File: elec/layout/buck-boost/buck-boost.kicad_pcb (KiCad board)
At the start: 6 copper layers, 69 parts, among them U10 2.49kΩ ±1% 62.5mW, U11 4.7µF ±10% 100V X7R, U12 4.7µF ±10% 100V X7R, U13 4.7µF ±10% 100V X7R, U14 10µF ±10% 100V X7R, U15 10µF ±10% 100V X7R, U16 10µF ±10% 100V X7R, U17 10µF ±10% 100V X7R, U18 1µF ±10% 100V X7R, U19 100nF ±10% 100V X7R, U2 100nF ±10% 50V X7R, U20 100pF ±5% 100V C0G, U21 470nF ±20% 16V X5R, U22 100nF ±10% 16V X7R, U23 10Ω ±1% 62.5mW, U24 100nF ±10% 16V X7R, U25 10Ω ±1% 62.5mW, U26 5mΩ ±1% 1W, U27 4.7µF ±10% 100V X7R, U28 4.7µF ±10% 100V X7R, U29 4.7µF ±10% 100V X7R, U3 100nF ±10% 50V X7R, U30 10µF ±10% 100V X7R, U31 10µF ±10% 100V X7R, U32 10µF ±10% 100V X7R, U33 10µF ±10% 100V X7R, U34 1µF ±10% 100V X7R, U35 100nF ±10% 100V X7R, U36 100pF ±5% 100V C0G, U37 470nF ±20% 16V X5R, U38 100nF ±10% 16V X7R, U39 10Ω ±1% 62.5mW, U4 50kΩ ±1% 62.5mW, U40 100nF ±10% 16V X7R, U41 10Ω ±1% 62.5mW, U42 5mΩ ±1% 1W, U43 13.7kΩ ±1% 62.5mW, U44 249kΩ ±0%, U45 1MΩ ±1% 100mW, U46 133kΩ ±1% 100mW, U47 25.5kΩ ±0% 100mW, U48 4.7µF ±10% 25V X5R, U49 100nF ±10% 100V X7R, U50 1µF ±10% 100V X7R, U51 4.7µF ±10% 100V X7R, U52 4.7µF ±10% 100V X7R, U54 0Ω 62.5mW, U58 30.1kΩ ±1% 62.5mW, U59 5.23kΩ ±1% 62.5mW, U9 4.7µF ±10% 25V X5R

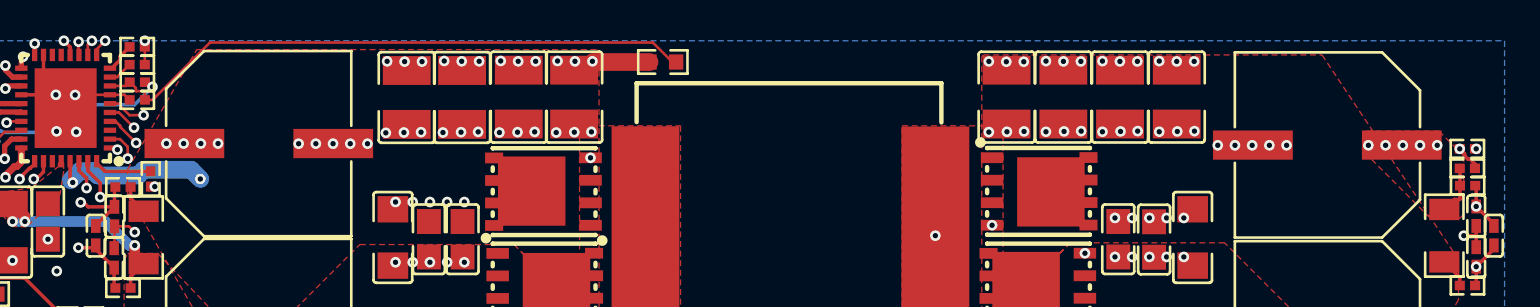
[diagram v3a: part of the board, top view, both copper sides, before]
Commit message: update syntax, delete vendored packages
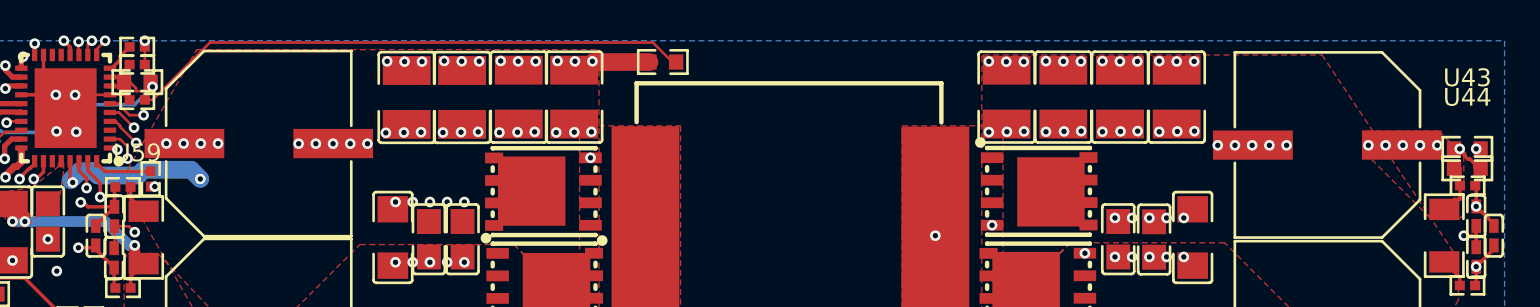
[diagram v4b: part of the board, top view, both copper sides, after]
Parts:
- U14, U15, U16, U17, U30, U31, U32, U33: value 10µF ±10% 100V X7R -> 10µF ±10% 100V X7S
- U43: value 13.7kΩ ±1% 62.5mW -> 13.7kΩ ±1% 100mW; footprint atopile:R0402-56259e -> atopile:R0603-ebcab9
- U44: value 249kΩ ±0% -> 249kΩ ±1% 100mW; footprint atopile:R0402-56259e -> atopile:R0603-ebcab9
- U59: value 5.23kΩ ±1% 62.5mW -> 5.23kΩ ±1% 100mW; footprint atopile:R0402-56259e -> atopile:R0603-ebcab9
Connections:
- C1 pad 1: hv-1 -> hv-3
- C2 pad 1: hv -> hv-2
- C3 pad 1: hv-3 -> hv-1
- C4 pad 1: hv-2 -> hv
- DS1 pad 1: cathode-1 -> cathode
- DS2 pad 1: cathode -> cathode-1
- Q1 pad 4: line-3 -> gate-2
- Q1 pad 5: hv-1 -> hv-3
- Q1 pad 6: hv-1 -> hv-3
- Q1 pad 7: hv-1 -> hv-3
- Q1 pad 8: hv-1 -> hv-3
- Q2 pad 4: line-6 -> gate
- Q3 pad 4: gate -> line-5
- Q3 pad 5: hv -> hv-2
- Q3 pad 6: hv -> hv-2
- Q3 pad 7: hv -> hv-2
- Q3 pad 8: hv -> hv-2
- R1 pad 2: gnd-4 -> gnd-1
- R2 pad 2: gnd-3 -> gnd-2
- R3 pad 2: gnd-2 -> gnd-4
- U1 pad 11: gnd-1 -> output_v_sense-gnd
- U1 pad 13: line -> line-3
- U1 pad 14: line-1 -> line
- U1 pad 19: gate -> line-5
- U1 pad 20: cathode -> cathode-1
- U1 pad 25: line-6 -> gate
- U1 pad 26: cathode-1 -> cathode
- U1 pad 27: line-3 -> gate-2
- U1 pad 30: line-5 -> line-1
- U1 pad 32: hv-3 -> hv-1
- U1 pad 33: hv-2 -> hv
- U1 pad 4: gnd-3 -> gnd-2
- U1 pad 5: gnd-2 -> gnd-4
- U1 pad 6: gnd-4 -> gnd-1
- U11 pad 1: hv-1 -> hv-3
- U12 pad 1: hv-1 -> hv-3
- U13 pad 1: hv-1 -> hv-3
- U14 pad 1: hv-1 -> hv-3
- U15 pad 1: hv-1 -> hv-3
- U16 pad 1: hv-1 -> hv-3
- U17 pad 1: hv-1 -> hv-3
- U18 pad 1: hv-1 -> hv-3
- U19 pad 1: hv-1 -> hv-3
- U2 pad 2: cathode-1 -> cathode
- U20 pad 1: hv-1 -> hv-3
- U21 pad 1: line-5 -> line-1
- U23 pad 1: hv-1 -> hv-3
- U24 pad 1: line-5 -> line-1
- U25 pad 1: hv-3 -> hv-1
- U25 pad 2: line-5 -> line-1
- U26 pad 1: hv-3 -> hv-1
- U26 pad 2: hv-1 -> hv-3
- U27 pad 1: hv -> hv-2
- U28 pad 1: hv -> hv-2
- U29 pad 1: hv -> hv-2
- U3 pad 2: cathode -> cathode-1
- U30 pad 1: hv -> hv-2
- U31 pad 1: hv -> hv-2
- U32 pad 1: hv -> hv-2
- U33 pad 1: hv -> hv-2
- U34 pad 1: hv -> hv-2
- U35 pad 1: hv -> hv-2
- U36 pad 1: hv -> hv-2
- U37 pad 1: line-1 -> line
- U37 pad 2: line -> line-3
- U38 pad 1: line -> line-3
- U39 pad 1: hv-2 -> hv
- U39 pad 2: line -> line-3
- U40 pad 1: line-1 -> line
- U41 pad 1: hv -> hv-2
- U41 pad 2: line-1 -> line
- U42 pad 1: hv -> hv-2
- U42 pad 2: hv-2 -> hv
- U43 pad 2: gnd-1 -> output_v_sense-gnd
- U44 pad 1: hv-2 -> hv
- U45 pad 1: hv-3 -> hv-1
- U49 pad 1: hv-3 -> hv-1
- U50 pad 1: hv-3 -> hv-1
- U51 pad 1: hv-1 -> hv-3
- U52 pad 1: hv -> hv-2
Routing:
- net output_v_sense-gnd: track 0.00 -> 81.7 mm, vias 0 -> 2
- net line-1: track 88.9 -> 10.1 mm
- net hv-2: track 78.8 -> 1.69 mm, vias 7 -> 34
- net hv: track 1.69 -> 78.8 mm, vias 34 -> 7
- net gnd-1: track 81.7 -> 17.4 mm
- net line-5: track 10.1 -> 59.3 mm
- net line-3: track 37.8 -> 86.4 mm
- net line-6: track 38.0 -> 0.00 mm, vias 2 -> 0
- net gate-2: track 0.00 -> 37.8 mm, vias 0 -> 2
- net hv-3: track 27.9 -> 1.67 mm, vias 8 -> 33
- net hv-1: track 1.67 -> 27.9 mm, vias 33 -> 8
- net gate: track 59.3 -> 38.0 mm
- net gnd-3: track 12.5 -> 0.00 mm, vias 2 -> 0
- net gnd-2: track 15.6 -> 12.5 mm
- net cathode-1: track 59.5 -> 62.4 mm
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- added copper zone on In2.Cu, net hv-2
- added copper zone on In2.Cu, net hv-3
- removed copper zone on In2.Cu, net hv
- removed copper zone on In2.Cu, net hv-1

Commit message: build and re-link layouts
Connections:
- net gnd-1 renamed gnd-3
- C1 pad 1: hv-3 -> hv-2
- C1 pad 2: gnd -> gnd-2
- C2 pad 1: hv-2 -> hv-1
- C2 pad 2: gnd -> gnd-2
- C3 pad 1: hv-1 -> hv
- C3 pad 2: gnd -> gnd-2
- C4 pad 1: hv -> hv-3
- C4 pad 2: gnd -> gnd-2
- DS1 pad 1: cathode -> cathode-1
- DS1 pad 2: anode -> anode-1
- DS2 pad 1: cathode-1 -> cathode
- DS2 pad 2: anode -> anode-1
- Q1 pad 4: gate-2 -> gate
- Q1 pad 5: hv-3 -> hv-2
- Q1 pad 6: hv-3 -> hv-2
- Q1 pad 7: hv-3 -> hv-2
- Q1 pad 8: hv-3 -> hv-2
- Q2 pad 1: gnd -> gnd-2
- Q2 pad 2: gnd -> gnd-2
- Q2 pad 3: gnd -> gnd-2
- Q2 pad 4: gate -> line-7
- Q3 pad 1: drain -> line-4
- Q3 pad 2: drain -> line-4
- Q3 pad 3: drain -> line-4
- Q3 pad 4: line-5 -> line
- Q3 pad 5: hv-2 -> hv-1
- Q3 pad 6: hv-2 -> hv-1
- Q3 pad 7: hv-2 -> hv-1
- Q3 pad 8: hv-2 -> hv-1
- Q4 pad 1: gnd -> gnd-2
- Q4 pad 2: gnd -> gnd-2
- Q4 pad 3: gnd -> gnd-2
- Q4 pad 5: drain -> line-4
- Q4 pad 6: drain -> line-4
- Q4 pad 7: drain -> line-4
- Q4 pad 8: drain -> line-4
- R2 pad 2: gnd-2 -> gnd-4
- R3 pad 2: gnd-4 -> gnd
- U1 pad 13: line-3 -> line-5
- U1 pad 14: line -> line-1
- U1 pad 17: gnd -> gnd-2
- U1 pad 18: drain -> line-4
- U1 pad 19: line-5 -> line
- U1 pad 20: cathode-1 -> cathode
- U1 pad 22: gnd -> gnd-2
- U1 pad 23: anode -> anode-1
- U1 pad 24: anode-1 -> anode
- U1 pad 25: gate -> line-7
- U1 pad 26: cathode -> cathode-1
- U1 pad 27: gate-2 -> gate
- U1 pad 29: line-4 -> line-3
- U1 pad 30: line-1 -> line-6
- U1 pad 32: hv-1 -> hv
- U1 pad 33: hv -> hv-3
- U1 pad 37: gnd -> gnd-2
- U1 pad 4: gnd-2 -> gnd-4
- U1 pad 5: gnd-4 -> gnd
- U1 pad 7: gnd -> gnd-2
- U10 pad 2: gnd -> gnd-2
- U11 pad 1: hv-3 -> hv-2
- U11 pad 2: gnd -> gnd-2
- U12 pad 1: hv-3 -> hv-2
- U12 pad 2: gnd -> gnd-2
- U13 pad 1: hv-3 -> hv-2
- U13 pad 2: gnd -> gnd-2
- U14 pad 1: hv-3 -> hv-2
- U14 pad 2: gnd -> gnd-2
- U15 pad 1: hv-3 -> hv-2
- U15 pad 2: gnd -> gnd-2
- U16 pad 1: hv-3 -> hv-2
- U16 pad 2: gnd -> gnd-2
- U17 pad 1: hv-3 -> hv-2
- U17 pad 2: gnd -> gnd-2
- U18 pad 1: hv-3 -> hv-2
- U18 pad 2: gnd -> gnd-2
- U19 pad 1: hv-3 -> hv-2
- U19 pad 2: gnd -> gnd-2
- U2 pad 2: cathode -> cathode-1
- U20 pad 1: hv-3 -> hv-2
- U20 pad 2: gnd -> gnd-2
- U21 pad 1: line-1 -> line-6
- U21 pad 2: line-4 -> line-3
- U22 pad 1: line-4 -> line-3
- U22 pad 2: gnd -> gnd-2
- U23 pad 1: hv-3 -> hv-2
- U23 pad 2: line-4 -> line-3
- U24 pad 1: line-1 -> line-6
- U24 pad 2: gnd -> gnd-2
- U25 pad 1: hv-1 -> hv
- U25 pad 2: line-1 -> line-6
- U26 pad 1: hv-1 -> hv
- U26 pad 2: hv-3 -> hv-2
- U27 pad 1: hv-2 -> hv-1
- U27 pad 2: gnd -> gnd-2
- U28 pad 1: hv-2 -> hv-1
- U28 pad 2: gnd -> gnd-2
- U29 pad 1: hv-2 -> hv-1
- U29 pad 2: gnd -> gnd-2
- U3 pad 1: drain -> line-4
- U3 pad 2: cathode-1 -> cathode
- U30 pad 1: hv-2 -> hv-1
- U30 pad 2: gnd -> gnd-2
- U31 pad 1: hv-2 -> hv-1
- U31 pad 2: gnd -> gnd-2
- U32 pad 1: hv-2 -> hv-1
- U32 pad 2: gnd -> gnd-2
- U33 pad 1: hv-2 -> hv-1
- U33 pad 2: gnd -> gnd-2
- U34 pad 1: hv-2 -> hv-1
- U34 pad 2: gnd -> gnd-2
- U35 pad 1: hv-2 -> hv-1
- U35 pad 2: gnd -> gnd-2
- U36 pad 1: hv-2 -> hv-1
- U36 pad 2: gnd -> gnd-2
- U37 pad 1: line -> line-1
- U37 pad 2: line-3 -> line-5
- U38 pad 1: line-3 -> line-5
- U38 pad 2: gnd -> gnd-2
- U39 pad 1: hv -> hv-3
- U39 pad 2: line-3 -> line-5
- U4 pad 2: gnd -> gnd-2
- U40 pad 1: line -> line-1
- U40 pad 2: gnd -> gnd-2
- U41 pad 1: hv-2 -> hv-1
- U41 pad 2: line -> line-1
- U42 pad 1: hv-2 -> hv-1
- U42 pad 2: hv -> hv-3
- U44 pad 1: hv -> hv-3
- U45 pad 1: hv-1 -> hv
- U47 pad 2: gnd -> gnd-2
- U48 pad 1: anode-1 -> anode
- U48 pad 2: gnd -> gnd-2
- U49 pad 1: hv-1 -> hv
- U49 pad 2: gnd -> gnd-2
- U5 pad 2: anode-1 -> anode
- U50 pad 1: hv-1 -> hv
- U50 pad 2: gnd -> gnd-2
- U51 pad 1: hv-3 -> hv-2
- U51 pad 2: gnd -> gnd-2
- U52 pad 1: hv-2 -> hv-1
- U52 pad 2: gnd -> gnd-2
- U54 pad 2: gnd -> gnd-2
- U55 pad 2: anode-1 -> anode
- U57 pad 2: gnd -> gnd-2
- U58 pad 2: gnd -> gnd-2
- U59 pad 1: anode-1 -> anode
- U7 pad 2: anode-1 -> anode
- U8 pad 2: drain -> line-4
- U9 pad 1: anode -> anode-1
- U9 pad 2: gnd -> gnd-2
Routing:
- net line-1: track 10.1 -> 88.9 mm
- net hv-3: track 1.67 -> 78.8 mm, vias 33 -> 7
- net line-3: track 86.4 -> 10.5 mm
- net drain: track 68.3 -> 0.00 mm, vias 2 -> 0
- net line-4: track 10.5 -> 68.3 mm
- net hv: track 78.8 -> 27.9 mm, vias 7 -> 8
- net line-7: track 0.00 -> 38.0 mm, vias 0 -> 2
- net gate-2: track 37.8 -> 0.00 mm, vias 2 -> 0
- net anode-1: track 35.4 -> 70.3 mm, vias 3 -> 2
- net anode: track 70.3 -> 35.4 mm, vias 2 -> 3
- net line: track 88.9 -> 59.3 mm
- net line-5: track 59.3 -> 86.4 mm
- net hv-1: track 27.9 -> 1.69 mm, vias 8 -> 34
- net gnd-2: track 12.5 -> 24.6 mm, vias 2 -> 90
- net line-6: track 0.00 -> 10.1 mm, vias 0 -> 2
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- added copper zone on B.Cu, net gnd-2
- added copper zone on F.Cu, net gnd-2
- added copper zone on In1.Cu, net gnd-2
- added copper zone on In2.Cu, net hv-1
- added copper zone on F.Cu, net line-4
- removed copper zone on F.Cu, net drain
- removed copper zone on B.Cu, net gnd
- removed copper zone on F.Cu, net gnd
- removed copper zone on In1.Cu, net gnd
- removed copper zone on In2.Cu, net hv-3

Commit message: all modules building
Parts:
- U50: value 1µF ±10% 100V X7R -> 1µF ±10% 250V X7R; footprint atopile:C1206-f0a137 -> atopile:C1812-bfe9b0
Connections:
- C1 pad 1: hv-2 -> hv-1
- C1 pad 2: gnd-2 -> gnd-3
- C2 pad 1: hv-1 -> hv-3
- C2 pad 2: gnd-2 -> gnd-3
- C3 pad 2: gnd-2 -> gnd-3
- C4 pad 1: hv-3 -> hv-2
- C4 pad 2: gnd-2 -> gnd-3
- DS1 pad 1: cathode-1 -> cathode
- DS2 pad 1: cathode -> cathode-1
- Q1 pad 1: line-2 -> drain
- Q1 pad 2: line-2 -> drain
- Q1 pad 3: line-2 -> drain
- Q1 pad 4: gate -> gate-2
- Q1 pad 5: hv-2 -> hv-1
- Q1 pad 6: hv-2 -> hv-1
- Q1 pad 7: hv-2 -> hv-1
- Q1 pad 8: hv-2 -> hv-1
- Q2 pad 1: gnd-2 -> gnd-3
- Q2 pad 2: gnd-2 -> gnd-3
- Q2 pad 3: gnd-2 -> gnd-3
- Q2 pad 4: line-7 -> gate
- Q2 pad 5: line-2 -> drain
- Q2 pad 6: line-2 -> drain
- Q2 pad 7: line-2 -> drain
- Q2 pad 8: line-2 -> drain
- Q3 pad 1: line-4 -> line
- Q3 pad 2: line-4 -> line
- Q3 pad 3: line-4 -> line
- Q3 pad 4: line -> gate-1
- Q3 pad 5: hv-1 -> hv-3
- Q3 pad 6: hv-1 -> hv-3
- Q3 pad 7: hv-1 -> hv-3
- Q3 pad 8: hv-1 -> hv-3
- Q4 pad 1: gnd-2 -> gnd-3
- Q4 pad 2: gnd-2 -> gnd-3
- Q4 pad 3: gnd-2 -> gnd-3
- Q4 pad 4: gate-1 -> line-4
- Q4 pad 5: line-4 -> line
- Q4 pad 6: line-4 -> line
- Q4 pad 7: line-4 -> line
- Q4 pad 8: line-4 -> line
- R1 pad 2: gnd-3 -> gnd-1
- U1 pad 13: line-5 -> line-1
- U1 pad 14: line-1 -> line-2
- U1 pad 17: gnd-2 -> gnd-3
- U1 pad 18: line-4 -> line
- U1 pad 19: line -> gate-1
- U1 pad 20: cathode -> cathode-1
- U1 pad 21: gate-1 -> line-4
- U1 pad 22: gnd-2 -> gnd-3
- U1 pad 25: line-7 -> gate
- U1 pad 26: cathode-1 -> cathode
- U1 pad 27: gate -> gate-2
- U1 pad 28: line-2 -> drain
- U1 pad 30: line-6 -> line-5
- U1 pad 33: hv-3 -> hv-2
- U1 pad 37: gnd-2 -> gnd-3
- U1 pad 6: gnd-3 -> gnd-1
- U1 pad 7: gnd-2 -> gnd-3
- U10 pad 2: gnd-2 -> gnd-3
- U11 pad 1: hv-2 -> hv-1
- U11 pad 2: gnd-2 -> gnd-3
- U12 pad 1: hv-2 -> hv-1
- U12 pad 2: gnd-2 -> gnd-3
- U13 pad 1: hv-2 -> hv-1
- U13 pad 2: gnd-2 -> gnd-3
- U14 pad 1: hv-2 -> hv-1
- U14 pad 2: gnd-2 -> gnd-3
- U15 pad 1: hv-2 -> hv-1
- U15 pad 2: gnd-2 -> gnd-3
- U16 pad 1: hv-2 -> hv-1
- U16 pad 2: gnd-2 -> gnd-3
- U17 pad 1: hv-2 -> hv-1
- U17 pad 2: gnd-2 -> gnd-3
- U18 pad 1: hv-2 -> hv-1
- U18 pad 2: gnd-2 -> gnd-3
- U19 pad 1: hv-2 -> hv-1
- U19 pad 2: gnd-2 -> gnd-3
- U2 pad 1: line-2 -> drain
- U2 pad 2: cathode-1 -> cathode
- U20 pad 1: hv-2 -> hv-1
- U20 pad 2: gnd-2 -> gnd-3
- U21 pad 1: line-6 -> line-5
- U22 pad 2: gnd-2 -> gnd-3
- U23 pad 1: hv-2 -> hv-1
- U24 pad 1: line-6 -> line-5
- U24 pad 2: gnd-2 -> gnd-3
- U25 pad 2: line-6 -> line-5
- U26 pad 2: hv-2 -> hv-1
- U27 pad 1: hv-1 -> hv-3
- U27 pad 2: gnd-2 -> gnd-3
- U28 pad 1: hv-1 -> hv-3
- U28 pad 2: gnd-2 -> gnd-3
- U29 pad 1: hv-1 -> hv-3
- U29 pad 2: gnd-2 -> gnd-3
- U3 pad 1: line-4 -> line
- U3 pad 2: cathode -> cathode-1
- U30 pad 1: hv-1 -> hv-3
- U30 pad 2: gnd-2 -> gnd-3
- U31 pad 1: hv-1 -> hv-3
- U31 pad 2: gnd-2 -> gnd-3
- U32 pad 1: hv-1 -> hv-3
- U32 pad 2: gnd-2 -> gnd-3
- U33 pad 1: hv-1 -> hv-3
- U33 pad 2: gnd-2 -> gnd-3
- U34 pad 1: hv-1 -> hv-3
- U34 pad 2: gnd-2 -> gnd-3
- U35 pad 1: hv-1 -> hv-3
- U35 pad 2: gnd-2 -> gnd-3
- U36 pad 1: hv-1 -> hv-3
- U36 pad 2: gnd-2 -> gnd-3
- U37 pad 1: line-1 -> line-2
- U37 pad 2: line-5 -> line-1
- U38 pad 1: line-5 -> line-1
- U38 pad 2: gnd-2 -> gnd-3
- U39 pad 1: hv-3 -> hv-2
- U39 pad 2: line-5 -> line-1
- U4 pad 2: gnd-2 -> gnd-3
- U40 pad 1: line-1 -> line-2
- U40 pad 2: gnd-2 -> gnd-3
- U41 pad 1: hv-1 -> hv-3
- U41 pad 2: line-1 -> line-2
- U42 pad 1: hv-1 -> hv-3
- U42 pad 2: hv-3 -> hv-2
- U44 pad 1: hv-3 -> hv-2
- U47 pad 2: gnd-2 -> gnd-3
- U48 pad 2: gnd-2 -> gnd-3
- U49 pad 2: gnd-2 -> gnd-3
- U50 pad 2: gnd-2 -> gnd-3
- U51 pad 1: hv-2 -> hv-1
- U51 pad 2: gnd-2 -> gnd-3
- U52 pad 1: hv-1 -> hv-3
- U52 pad 2: gnd-2 -> gnd-3
- U54 pad 2: gnd-2 -> gnd-3
- U57 pad 2: gnd-2 -> gnd-3
- U58 pad 2: gnd-2 -> gnd-3
- U8 pad 1: line-2 -> drain
- U8 pad 2: line-4 -> line
- U9 pad 2: gnd-2 -> gnd-3
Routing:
- net hv-2: track 1.67 -> 78.8 mm, vias 33 -> 7
- net hv-3: track 78.8 -> 1.69 mm, vias 7 -> 34
- net line-5: track 86.4 -> 10.1 mm
- net drain: track 0.00 -> 55.2 mm, vias 0 -> 3
- net line-7: track 38.0 -> 0.00 mm, vias 2 -> 0
- net gate-2: track 0.00 -> 37.8 mm, vias 0 -> 2
- net line-2: track 55.2 -> 88.9 mm, vias 3 -> 2
- net gnd-2: track 24.6 -> 0.00 mm, vias 90 -> 0
- net gnd-1: track 0.00 -> 17.4 mm, vias 0 -> 2
- net line-6: track 10.1 -> 0.00 mm, vias 2 -> 0
- net line: track 59.3 -> 68.3 mm
- net gate-1: track 67.3 -> 59.3 mm
- net gnd-3: track 17.4 -> 24.6 mm, vias 2 -> 90
- net cathode-1: track 59.5 -> 62.4 mm
- net cathode: track 62.4 -> 59.5 mm
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- added copper zone on F.Cu, net drain
- added copper zone on B.Cu, net gnd-3
- added copper zone on F.Cu, net gnd-3
- added copper zone on In1.Cu, net gnd-3
- added copper zone on In2.Cu, net hv-3
- added copper zone on F.Cu, net line
- removed copper zone on B.Cu, net gnd-2
- removed copper zone on F.Cu, net gnd-2
- removed copper zone on In1.Cu, net gnd-2
- removed copper zone on In2.Cu, net hv-2
- removed copper zone on F.Cu, net line-2
- removed copper zone on F.Cu, net line-4

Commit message: HIL Building
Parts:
- U43: value 13.7kΩ ±1% 100mW -> 13.7kΩ ±1% 62.5mW; footprint atopile:R0603-ebcab9 -> atopile:R0402-56259e
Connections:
- net gate-1 renamed line-6
- C1 pad 1: hv-1 -> hv
- C1 pad 2: gnd-3 -> gnd
- C2 pad 1: hv-3 -> hv-1
- C2 pad 2: gnd-3 -> gnd
- C3 pad 1: hv -> hv-3
- C3 pad 2: gnd-3 -> gnd
- C4 pad 2: gnd-3 -> gnd
- DS1 pad 1: cathode -> cathode-1
- DS2 pad 1: cathode-1 -> cathode
- Q1 pad 1: drain -> source
- Q1 pad 2: drain -> source
- Q1 pad 3: drain -> source
- Q1 pad 4: gate-2 -> line
- Q1 pad 5: hv-1 -> hv
- Q1 pad 6: hv-1 -> hv
- Q1 pad 7: hv-1 -> hv
- Q1 pad 8: hv-1 -> hv
- Q2 pad 1: gnd-3 -> gnd
- Q2 pad 2: gnd-3 -> gnd
- Q2 pad 3: gnd-3 -> gnd
- Q2 pad 4: gate -> line-2
- Q2 pad 5: drain -> source
- Q2 pad 6: drain -> source
- Q2 pad 7: drain -> source
- Q2 pad 8: drain -> source
- Q3 pad 1: line -> drain
- Q3 pad 2: line -> drain
- Q3 pad 3: line -> drain
- Q3 pad 5: hv-3 -> hv-1
- Q3 pad 6: hv-3 -> hv-1
- Q3 pad 7: hv-3 -> hv-1
- Q3 pad 8: hv-3 -> hv-1
- Q4 pad 1: gnd-3 -> gnd
- Q4 pad 2: gnd-3 -> gnd
- Q4 pad 3: gnd-3 -> gnd
- Q4 pad 4: line-4 -> gate
- Q4 pad 5: line -> drain
- Q4 pad 6: line -> drain
- Q4 pad 7: line -> drain
- Q4 pad 8: line -> drain
- R1 pad 2: gnd-1 -> gnd-2
- R2 pad 2: gnd-4 -> gnd-3
- R3 pad 2: gnd -> gnd-4
- U1 pad 11: output_v_sense-gnd -> gnd-1
- U1 pad 13: line-1 -> line-3
- U1 pad 14: line-2 -> line-1
- U1 pad 17: gnd-3 -> gnd
- U1 pad 18: line -> drain
- U1 pad 20: cathode-1 -> cathode
- U1 pad 21: line-4 -> gate
- U1 pad 22: gnd-3 -> gnd
- U1 pad 25: gate -> line-2
- U1 pad 26: cathode -> cathode-1
- U1 pad 27: gate-2 -> line
- U1 pad 28: drain -> source
- U1 pad 29: line-3 -> line-4
- U1 pad 32: hv -> hv-3
- U1 pad 37: gnd-3 -> gnd
- U1 pad 4: gnd-4 -> gnd-3
- U1 pad 5: gnd -> gnd-4
- U1 pad 6: gnd-1 -> gnd-2
- U1 pad 7: gnd-3 -> gnd
- U10 pad 2: gnd-3 -> gnd
- U11 pad 1: hv-1 -> hv
- U11 pad 2: gnd-3 -> gnd
- U12 pad 1: hv-1 -> hv
- U12 pad 2: gnd-3 -> gnd
- U13 pad 1: hv-1 -> hv
- U13 pad 2: gnd-3 -> gnd
- U14 pad 1: hv-1 -> hv
- U14 pad 2: gnd-3 -> gnd
- U15 pad 1: hv-1 -> hv
- U15 pad 2: gnd-3 -> gnd
- U16 pad 1: hv-1 -> hv
- U16 pad 2: gnd-3 -> gnd
- U17 pad 1: hv-1 -> hv
- U17 pad 2: gnd-3 -> gnd
- U18 pad 1: hv-1 -> hv
- U18 pad 2: gnd-3 -> gnd
- U19 pad 1: hv-1 -> hv
- U19 pad 2: gnd-3 -> gnd
- U2 pad 1: drain -> source
- U2 pad 2: cathode -> cathode-1
- U20 pad 1: hv-1 -> hv
- U20 pad 2: gnd-3 -> gnd
- U21 pad 2: line-3 -> line-4
- U22 pad 1: line-3 -> line-4
- U22 pad 2: gnd-3 -> gnd
- U23 pad 1: hv-1 -> hv
- U23 pad 2: line-3 -> line-4
- U24 pad 2: gnd-3 -> gnd
- U25 pad 1: hv -> hv-3
- U26 pad 1: hv -> hv-3
- U26 pad 2: hv-1 -> hv
- U27 pad 1: hv-3 -> hv-1
- U27 pad 2: gnd-3 -> gnd
- U28 pad 1: hv-3 -> hv-1
- U28 pad 2: gnd-3 -> gnd
- U29 pad 1: hv-3 -> hv-1
- U29 pad 2: gnd-3 -> gnd
- U3 pad 1: line -> drain
- U3 pad 2: cathode-1 -> cathode
- U30 pad 1: hv-3 -> hv-1
- U30 pad 2: gnd-3 -> gnd
- U31 pad 1: hv-3 -> hv-1
- U31 pad 2: gnd-3 -> gnd
- U32 pad 1: hv-3 -> hv-1
- U32 pad 2: gnd-3 -> gnd
- U33 pad 1: hv-3 -> hv-1
- U33 pad 2: gnd-3 -> gnd
- U34 pad 1: hv-3 -> hv-1
- U34 pad 2: gnd-3 -> gnd
- U35 pad 1: hv-3 -> hv-1
- U35 pad 2: gnd-3 -> gnd
- U36 pad 1: hv-3 -> hv-1
- U36 pad 2: gnd-3 -> gnd
- U37 pad 1: line-2 -> line-1
- U37 pad 2: line-1 -> line-3
- U38 pad 1: line-1 -> line-3
- U38 pad 2: gnd-3 -> gnd
- U39 pad 2: line-1 -> line-3
- U4 pad 2: gnd-3 -> gnd
- U40 pad 1: line-2 -> line-1
- U40 pad 2: gnd-3 -> gnd
- U41 pad 1: hv-3 -> hv-1
- U41 pad 2: line-2 -> line-1
- U42 pad 1: hv-3 -> hv-1
- U43 pad 2: output_v_sense-gnd -> gnd-1
- U45 pad 1: hv -> hv-3
- U47 pad 2: gnd-3 -> gnd
- U48 pad 2: gnd-3 -> gnd
- U49 pad 1: hv -> hv-3
- U49 pad 2: gnd-3 -> gnd
- U50 pad 1: hv -> hv-3
- U50 pad 2: gnd-3 -> gnd
- U51 pad 1: hv-1 -> hv
- U51 pad 2: gnd-3 -> gnd
- U52 pad 1: hv-3 -> hv-1
- U52 pad 2: gnd-3 -> gnd
- U54 pad 2: gnd-3 -> gnd
- U57 pad 2: gnd-3 -> gnd
- U58 pad 2: gnd-3 -> gnd
- U8 pad 1: drain -> source
- U8 pad 2: line -> drain
- U9 pad 2: gnd-3 -> gnd
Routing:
- net output_v_sense-gnd: track 81.7 -> 0.00 mm, vias 2 -> 0
- net line-3: track 10.5 -> 86.4 mm
- net gnd-1: track 17.4 -> 81.7 mm
- net line-4: track 67.3 -> 10.5 mm
- net source: track 0.00 -> 55.2 mm, vias 0 -> 3
- net line-2: track 88.9 -> 38.0 mm
- net gate-2: track 37.8 -> 0.00 mm, vias 2 -> 0
- net line: track 68.3 -> 37.8 mm
- net gate: track 38.0 -> 67.3 mm
- net hv: track 27.9 -> 1.67 mm, vias 8 -> 33
- net hv-3: track 1.69 -> 27.9 mm, vias 34 -> 8
- net gnd-2: track 0.00 -> 17.4 mm, vias 0 -> 2
- net drain: track 55.2 -> 68.3 mm, vias 3 -> 2
- net gnd-3: track 24.6 -> 12.5 mm, vias 90 -> 2
- net gnd: track 15.6 -> 24.6 mm, vias 2 -> 90
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- added copper zone on B.Cu, net gnd
- added copper zone on F.Cu, net gnd
- added copper zone on In1.Cu, net gnd
- added copper zone on In2.Cu, net hv
- added copper zone on F.Cu, net source
- removed copper zone on B.Cu, net gnd-3
- removed copper zone on F.Cu, net gnd-3
- removed copper zone on In1.Cu, net gnd-3
- removed copper zone on In2.Cu, net hv-3
- removed copper zone on F.Cu, net line
